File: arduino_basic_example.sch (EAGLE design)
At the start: 23 parts, among them IC1 ATMEGA328P, Q1 16mhz

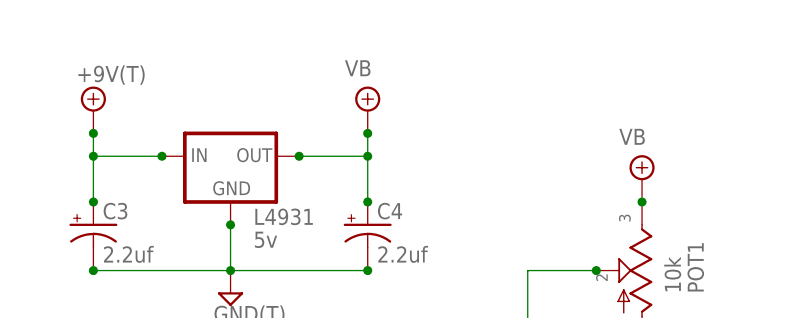
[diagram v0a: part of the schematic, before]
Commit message: update regulator label
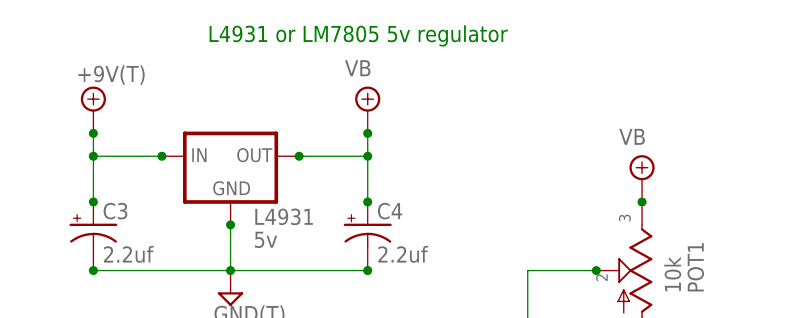
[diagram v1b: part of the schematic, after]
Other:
- note added: "L4931 or LM7805 5v regulator"
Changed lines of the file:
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@@
 <sheet>
 <plain>
+<text x="73.66" y="114.3" size="1.778" layer="91">L4931 or LM7805 5v regulator</text>
 </plain>
 <instances>

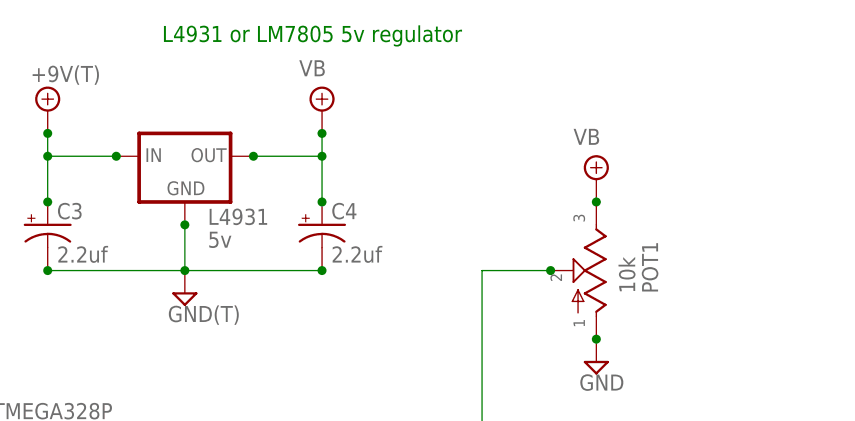
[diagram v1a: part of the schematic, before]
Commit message: update regulator label
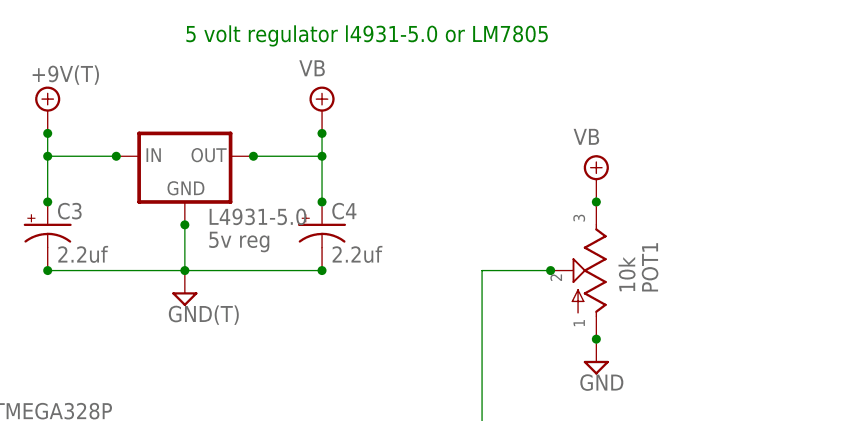
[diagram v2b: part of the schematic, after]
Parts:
- L4931-5.0: value 5v -> 5v reg
- renumbered L4931 to L4931-5.0
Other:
- note added: "5 volt regulator l4931-5.0 or LM7805"
- note removed: "L4931 or LM7805 5v regulator"
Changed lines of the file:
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@@
 <parts>
 <part name="IC1" library="atmel" deviceset="MEGA8-P" device="" value="ATMEGA328P"/>
-<part name="L4931" library="v-reg-3" deviceset="78LXX" device="" value="5v"/>
+<part name="L4931-5.0" library="v-reg-3" deviceset="78LXX" device="" value="5v reg"/>
 <part name="R1" library="gm-resistors" deviceset="6MM" device=".3" value="10k"/>
 <part name="GND1" library="gm-supply" deviceset="GND(T)" device=""/>
@@
 <sheet>
 <plain>
-<text x="73.66" y="114.3" size="1.778" layer="91">L4931 or LM7805 5v regulator</text>
+<text x="76.2" y="114.3" size="1.778" layer="91">5 volt regulator l4931-5.0 or LM7805</text>
 </plain>
 <instances>
 <instance part="IC1" gate="G$1" x="71.12" y="40.64"/>
-<instance part="L4931" gate="1" x="76.2" y="101.6"/>
+<instance part="L4931-5.0" gate="1" x="76.2" y="101.6"/>
 <instance part="R1" gate="G$1" x="48.26" y="78.74" rot="R90"/>
 <instance part="GND1" gate="GND" x="76.2" y="86.36"/>
@@
 </segment>
 <segment>
-<pinref part="L4931" gate="1" pin="OUT"/>
+<pinref part="L4931-5.0" gate="1" pin="OUT"/>
 <pinref part="VB1" gate="G$1" pin="VB"/>
 <wire x1="83.82" y1="101.6" x2="91.44" y2="101.6" width="0.1524" layer="91"/>
@@
 <segment>
 <pinref part="GND1" gate="GND" pin="GND"/>
-<pinref part="L4931" gate="1" pin="GND"/>
+<pinref part="L4931-5.0" gate="1" pin="GND"/>
 <wire x1="76.2" y1="88.9" x2="76.2" y2="93.98" width="0.1524" layer="91"/>
 <junction x="76.2" y="93.98"/>
@@
 <segment>
 <pinref part="+9V1" gate="+9V" pin="+9V"/>
-<pinref part="L4931" gate="1" pin="IN"/>
+<pinref part="L4931-5.0" gate="1" pin="IN"/>
 <wire x1="60.96" y1="104.14" x2="60.96" y2="101.6" width="0.1524" layer="91"/>
 <wire x1="60.96" y1="101.6" x2="68.58" y2="101.6" width="0.1524" layer="91"/>
